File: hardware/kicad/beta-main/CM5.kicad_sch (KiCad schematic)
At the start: 1 part, among them J1 FFC3A20-15-G

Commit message: tweaks and added servo controller
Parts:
- added J2, J3, J4, J5: Servo Socket, symbol Connector:Conn_01x03_Pin
- added Q1: MMBT3906, Package_TO_SOT_SMD:SOT-23, symbol Transistor_BJT:MMBT3906
- added R1, R2, R4, R5: 10k, symbol Device:R
- added R3: 20k, symbol Device:R
- added U1, U2: 74LVC1G126, symbol Beta:74LVC1G126
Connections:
- net 3V3: now also Q1.2 (E), R1.1, R4.1, R5.1, U1.5 (VCC), U2.5 (VCC)
- net GND: now also J2.3 (Pin_3), J3.3 (Pin_3), J4.3 (Pin_3), J5.3 (Pin_3), R3.1, U1.3 (GND), U2.3 (GND)
- new net: J2.1 (Pin_1), J3.1 (Pin_1), J4.1 (Pin_1), J5.1 (Pin_1), R4.2, U1.4, U2.2
- new net: Q1.1 (B), R2.1
- new net 12V: J2.2 (Pin_2), J3.2 (Pin_2), J4.2 (Pin_2), J5.2 (Pin_2)
- new net TXEN: Q1.3 (C), R3.2, U1.1, U2.1
- new net UART3_RX: R5.2, U2.4
- new net UART3_TX: R1.2, R2.2, U1.2
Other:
- sheet GPIO ports: added UART3_RX, UART3_TX; removed none
- note added: "Servo Controller"

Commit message: tweaks
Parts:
- added J6: FFC3A20-15-G, symbol Connector:Conn_01x15_Socket
- U1, U2: Supplier (none) -> https://www.tme.eu/en/details/sn74lvc1g126dbvr/buffers-tran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
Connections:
- net 3V3: now also J6.15 (Pin_15)
- net GND: now also J6.1 (Pin_1), J6.10 (Pin_10), J6.4 (Pin_4), J6.7 (Pin_7)
- new net MIPI1_C_N: J6.8 (Pin_8)
- new net MIPI1_C_P: J6.9 (Pin_9)
- new net MIPI1_D0_N: J6.2 (Pin_2)
- new net MIPI1_D0_P: J6.3 (Pin_3)
- new net MIPI1_D1_N: J6.5 (Pin_5)
- new net MIPI1_D1_P: J6.6 (Pin_6)
- new net SCL1: J6.13 (Pin_13)
- new net SDA1: J6.14 (Pin_14)
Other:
- sheet GPIO ports: added CAM_GPIO0, CAM_GPIO1, SCL1, SDA1; removed none

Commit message: sync changes after meeting
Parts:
- removed J2, J3, J4, J5: Servo Socket, symbol Connector:Conn_01x03_Pin
- removed Q1: MMBT3906, Package_TO_SOT_SMD:SOT-23, symbol Transistor_BJT:MMBT3906
- removed R1, R2, R4, R5: 10k, symbol Device:R
- removed R3: 20k, symbol Device:R
- removed U1, U2: 74LVC1G126, symbol Beta:74LVC1G126
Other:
- note removed: "Servo Controller"

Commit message: Wzmacniacz dodany
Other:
- sheet GPIO ports: added GPIO18, GPIO19, GPIO21; removed none
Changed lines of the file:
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@@
+	(wire
+		(pts
+			(xy 48.26 41.91) (xy 57.15 41.91)
+		)
+		(stroke
+			(width 0)
+			(type default)
+		)
+	)
 	(wire
 		(pts
@@
 	(wire
 		(pts
+			(xy 48.26 44.45) (xy 57.15 44.45)
+		)
+		(stroke
+			(width 0)
+			(type default)
+		)
+	)
+	(wire
+		(pts
 			(xy 231.14 92.71) (xy 241.3 92.71)
 		)
@@
 		(pts
 			(xy 161.29 49.53) (xy 158.75 49.53)
+		)
+		(stroke
+			(width 0)
+			(type default)
+		)
+	)
+	(wire
+		(pts
+			(xy 48.26 39.37) (xy 57.15 39.37)
 		)
 		(stroke
@@
 		)
 	)
+	(hierarchical_label "GPIO18"
+		(shape input)
+		(at 48.26 39.37 180)
+		(effects
+			(font
+				(size 1.27 1.27)
+			)
+			(justify right)
+		)
+	)
 	(hierarchical_label "GND"
 		(shape input)
@@
 		)
 	)
+	(hierarchical_label "GPIO19"
+		(shape input)
+		(at 48.26 41.91 180)
+		(effects
+			(font
+				(size 1.27 1.27)
+			)
+			(justify right)
+		)
+	)
 	(hierarchical_label "5V"
 		(shape input)
 		(at 52.07 54.61 180)
+		(effects
+			(font
+				(size 1.27 1.27)
+			)
+			(justify right)
+		)
+	)
+	(hierarchical_label "GPIO21"
+		(shape input)
+		(at 48.26 44.45 180)
 		(effects
 			(font
@@
 			)
 		)
+		(pin "GPIO19" input
+			(at 57.15 41.91 180)
+			(effects
+				(font
+					(size 1.27 1.27)
+				)
+				(justify left)
+			)
+		)
+		(pin "GPIO18" input
+			(at 57.15 39.37 180)
+			(effects
+				(font
+					(size 1.27 1.27)
+				)
+				(justify left)
+			)
+		)
+		(pin "GPIO21" input
+			(at 57.15 44.45 180)
+			(effects
+				(font
+					(size 1.27 1.27)
+				)
+				(justify left)
+			)
+		)

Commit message: 5V and amplifier corrections
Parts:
- renumbered J6 to J2
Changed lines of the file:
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@@
 		(dnp no)
 		(fields_autoplaced yes)
-		(property "Reference" "J6"
+		(property "Reference" "J2"
 			(at 247.65 104.1399 0)
 			(effects
@@
 			(project "beta-main"
 				(path "/ec75fd42-4efa-4f32-b57e-76d632cb46f5/b3cf40a7-4d41-420e-a440-2c08f4160b31"
-					(reference "J6")
+					(reference "J2")
 					(unit 1)
 				)

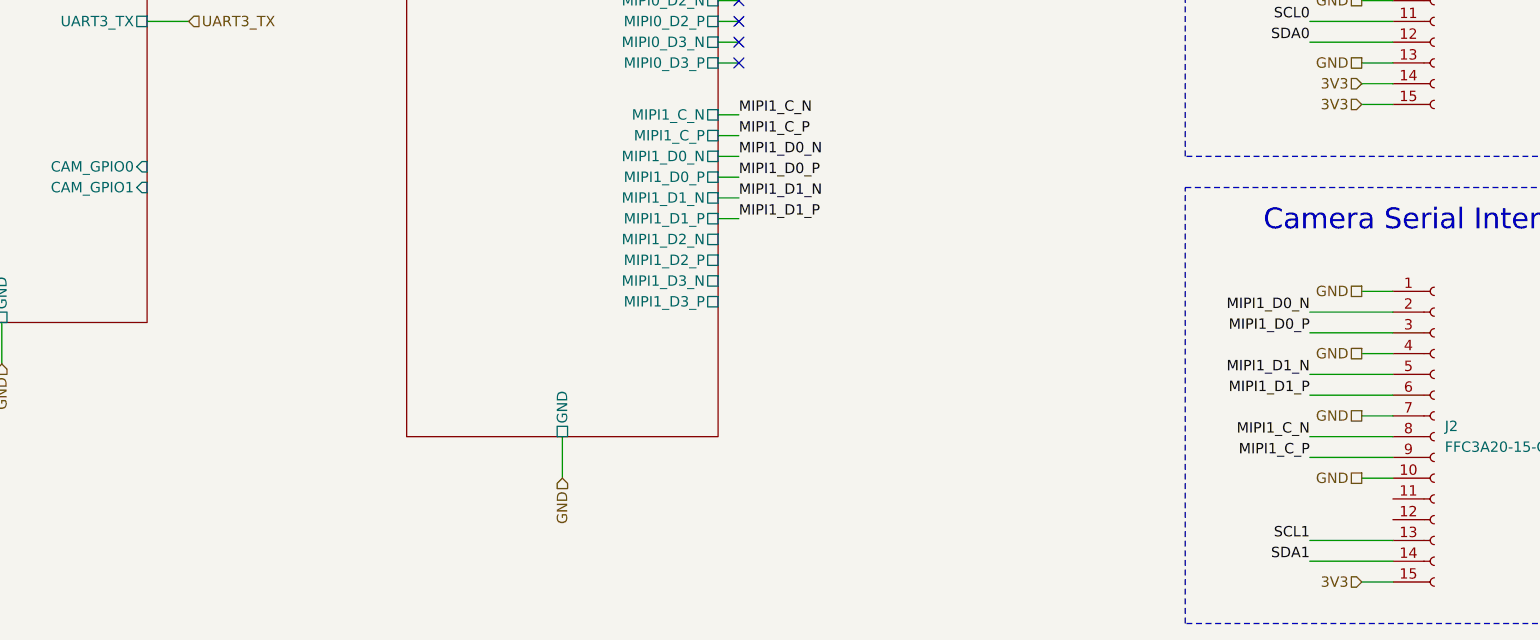
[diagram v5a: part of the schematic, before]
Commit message: Amplifier set for left channel only and god rid of all errors from ERC
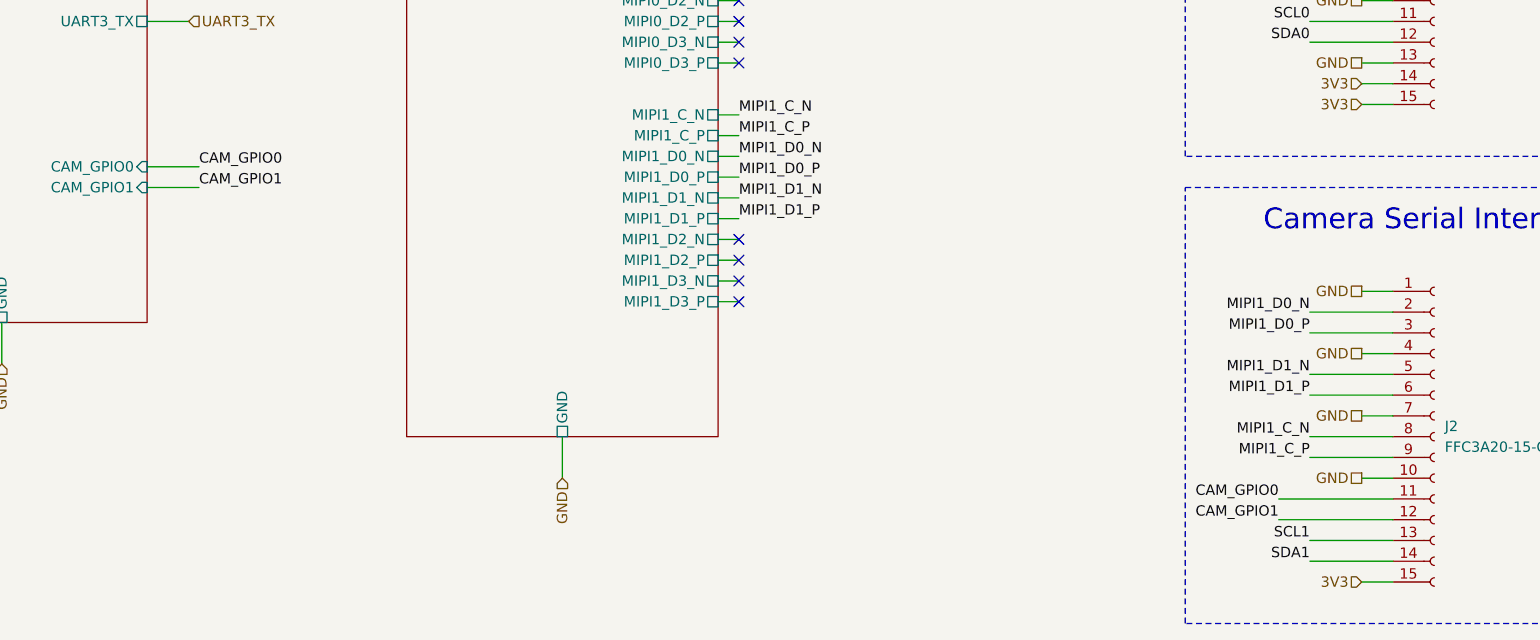
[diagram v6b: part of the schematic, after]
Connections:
- net CAM_GPIO0: now reaches J2.11 (Pin_11)
- net CAM_GPIO1: now reaches J2.12 (Pin_12)
- no-connect marks 4 -> 8
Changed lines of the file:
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@@
+	)
+	(no_connect
+		(at 161.29 88.9)
+	)
+	(no_connect
+		(at 161.29 81.28)
+	)
+	(no_connect
+		(at 161.29 83.82)
+	)
+	(no_connect
+		(at 161.29 86.36)
 	)
 	(no_connect
@@
 	(wire
 		(pts
+			(xy 88.9 74.93) (xy 95.25 74.93)
+		)
+		(stroke
+			(width 0)
+			(type default)
+		)
+	)
+	(wire
+		(pts
+			(xy 88.9 72.39) (xy 95.25 72.39)
+		)
+		(stroke
+			(width 0)
+			(type default)
+		)
+	)
+	(wire
+		(pts
 			(xy 231.14 97.79) (xy 241.3 97.79)
 		)
@@
 	(wire
 		(pts
+			(xy 158.75 81.28) (xy 161.29 81.28)
+		)
+		(stroke
+			(width 0)
+			(type default)
+		)
+	)
+	(wire
+		(pts
 			(xy 231.14 92.71) (xy 241.3 92.71)
 		)
@@
 	(wire
 		(pts
+			(xy 227.33 113.03) (xy 241.3 113.03)
+		)
+		(stroke
+			(width 0)
+			(type default)
+		)
+	)
+	(wire
+		(pts
 			(xy 48.26 39.37) (xy 57.15 39.37)
 		)
@@
 	(wire
 		(pts
+			(xy 158.75 88.9) (xy 161.29 88.9)
+		)
+		(stroke
+			(width 0)
+			(type default)
+		)
+	)
+	(wire
+		(pts
 			(xy 158.75 59.69) (xy 161.29 59.69)
 		)
@@
 	(wire
 		(pts
+			(xy 158.75 86.36) (xy 161.29 86.36)
+		)
+		(stroke
+			(width 0)
+			(type default)
+		)
+	)
+	(wire
+		(pts
 			(xy 161.29 39.37) (xy 158.75 39.37)
 		)
@@
 	(wire
 		(pts
+			(xy 227.33 115.57) (xy 241.3 115.57)
+		)
+		(stroke
+			(width 0)
+			(type default)
+		)
+	)
+	(wire
+		(pts
 			(xy 237.49 110.49) (xy 241.3 110.49)
 		)
@@
 		(pts
 			(xy 237.49 102.87) (xy 241.3 102.87)
+		)
+		(stroke
+			(width 0)
+			(type default)
+		)
+	)
+	(wire
+		(pts
+			(xy 158.75 83.82) (xy 161.29 83.82)
 		)
 		(stroke
@@
 		)
 	)
+	(label "CAM_GPIO0"
+		(at 227.33 113.03 180)
+		(effects
+			(font
+				(size 1.27 1.27)
+			)
+			(justify right bottom)
+		)
+	)
 	(label "MIPI0_C_N"
 		(at 161.29 36.83 0)
@@
 		)
 	)
+	(label "CAM_GPIO0"
+		(at 95.25 72.39 0)
+		(effects
+			(font
+				(size 1.27 1.27)
+			)
+			(justify left bottom)
+		)
+	)
 	(label "SDA1"
 		(at 231.14 120.65 180)
@@
 		)
 	)
+	(label "CAM_GPIO1"
+		(at 95.25 74.93 0)
+		(effects
+			(font
+				(size 1.27 1.27)
+			)
+			(justify left bottom)
+		)
+	)
 	(label "MIPI1_D0_P"
 		(at 231.14 92.71 180)
@@
 		)
 	)
+	(label "CAM_GPIO1"
+		(at 227.33 115.57 180)
+		(effects
+			(font
+				(size 1.27 1.27)
+			)
+			(justify right bottom)
+		)
+	)

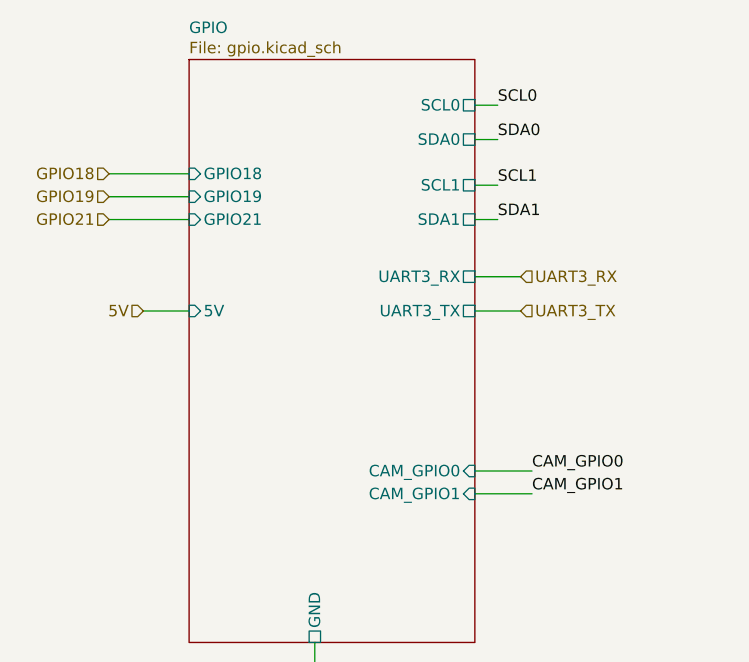
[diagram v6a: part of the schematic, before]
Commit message: Gyroscope added without errors in ERC
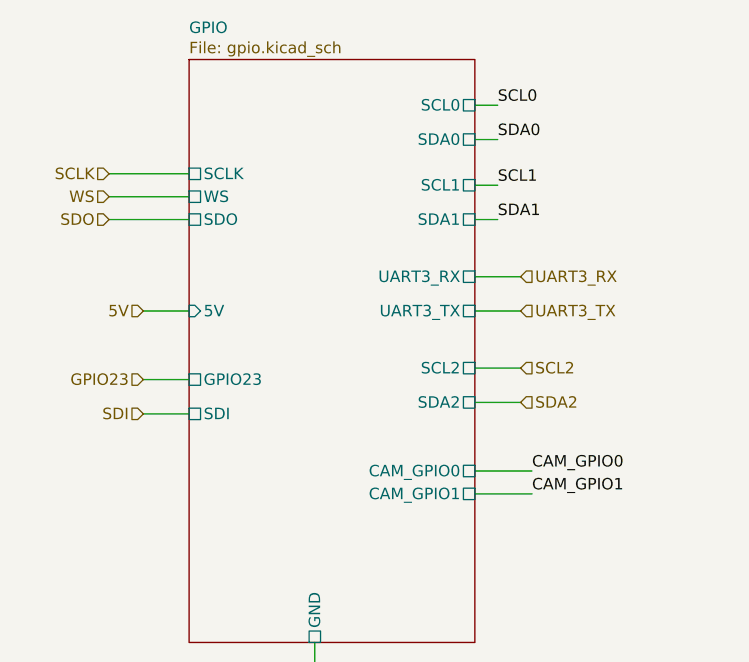
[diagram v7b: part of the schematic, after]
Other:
- sheet GPIO ports: added GPIO23, SCL2, SCLK, SDA2, SDI, SDO, WS; removed GPIO18, GPIO19, GPIO21
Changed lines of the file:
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@@
+	(wire
+		(pts
+			(xy 93.98 64.77) (xy 88.9 64.77)
+		)
+		(stroke
+			(width 0)
+			(type default)
+		)
+	)
 	(wire
 		(pts
@@
 	(wire
 		(pts
+			(xy 52.07 66.04) (xy 57.15 66.04)
+		)
+		(stroke
+			(width 0)
+			(type default)
+		)
+	)
+	(wire
+		(pts
 			(xy 158.75 59.69) (xy 161.29 59.69)
 		)
@@
 		(pts
 			(xy 158.75 83.82) (xy 161.29 83.82)
+		)
+		(stroke
+			(width 0)
+			(type default)
+		)
+	)
+	(wire
+		(pts
+			(xy 52.07 62.23) (xy 57.15 62.23)
+		)
+		(stroke
+			(width 0)
+			(type default)
+		)
+	)
+	(wire
+		(pts
+			(xy 88.9 60.96) (xy 93.98 60.96)
 		)
 		(stroke
@@
 		)
 	)
+	(hierarchical_label "GPIO23"
+		(shape input)
+		(at 52.07 62.23 180)
+		(effects
+			(font
+				(size 1.27 1.27)
+			)
+			(justify right)
+		)
+	)
+	(hierarchical_label "SDA2"
+		(shape input)
+		(at 93.98 64.77 0)
+		(effects
+			(font
+				(size 1.27 1.27)
+			)
+			(justify left)
+		)
+	)
 	(hierarchical_label "GND"
 		(shape passive)
@@
 		)
 	)
-	(hierarchical_label "GPIO18"
+	(hierarchical_label "SCLK"
 		(shape input)
 		(at 48.26 39.37 180)
@@
 		)
 	)
+	(hierarchical_label "SDI"
+		(shape input)
+		(at 52.07 66.04 180)
+		(effects
+			(font
+				(size 1.27 1.27)
+			)
+			(justify right)
+		)
+	)
 	(hierarchical_label "3V3"
 		(shape input)
@@
 		)
 	)
-	(hierarchical_label "GPIO19"
+	(hierarchical_label "WS"
 		(shape input)
 		(at 48.26 41.91 180)
@@
 		)
 	)
-	(hierarchical_label "GPIO21"
+	(hierarchical_label "SDO"
 		(shape input)
 		(at 48.26 44.45 180)
@@
 		(shape input)
 		(at 93.98 54.61 0)
+		(effects
+			(font
+				(size 1.27 1.27)
+			)
+			(justify left)
+		)
+	)
+	(hierarchical_label "SCL2"
+		(shape input)
+		(at 93.98 60.96 0)
 		(effects
 			(font
@@
 			)
 		)
-		(pin "CAM_GPIO0" input
-			(at 88.9 72.39 0)
-			(effects
-				(font
-					(size 1.27 1.27)
-				)
-				(justify right)
-			)
-		)
-		(pin "CAM_GPIO1" input
-			(at 88.9 74.93 0)
-			(effects
-				(font
-					(size 1.27 1.27)
-				)
-				(justify right)
-			)
-		)
 		(pin "SCL1" passive
 			(at 88.9 40.64 0)
@@
 			)
 		)
-		(pin "GPIO19" input
+		(pin "SDA2" passive
+			(at 88.9 64.77 0)
+			(effects
+				(font
+					(size 1.27 1.27)
+				)
+				(justify right)
+			)
+		)
+		(pin "SCL2" passive
+			(at 88.9 60.96 0)
+			(effects
+				(font
+					(size 1.27 1.27)
+				)
+				(justify right)
+			)
+		)
+		(pin "SCLK" passive
+			(at 57.15 39.37 180)
+			(effects
+				(font
+					(size 1.27 1.27)
+				)
+				(justify left)
+			)
+		)
+		(pin "WS" passive
 			(at 57.15 41.91 180)
 			(effects
@@
 			)
 		)
-		(pin "GPIO18" input
-			(at 57.15 39.37 180)
+		(pin "SDO" passive
+			(at 57.15 44.45 180)
 			(effects
 				(font
@@
 			)
 		)
-		(pin "GPIO21" input
-			(at 57.15 44.45 180)
-			(effects
-				(font
+		(pin "CAM_GPIO0" passive
+			(at 88.9 72.39 0)
+			(effects
+				(font
+					(size 1.27 1.27)
+				)
+				(justify right)
+			)
+		)
+		(pin "CAM_GPIO1" passive
+			(at 88.9 74.93 0)
+			(effects
+				(font
+					(size 1.27 1.27)
+				)
+				(justify right)
+			)
+		)
+		(pin "GPIO23" passive
+			(at 57.15 62.23 180)
+			(effects
+				(font
+					(size 1.27 1.27)
+				)
+				(justify left)
+			)
+		)
+		(pin "SDI" passive
+			(at 57.15 66.04 180)
+			(effects
+				(font

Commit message: Setup for PCB layout
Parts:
- J1, J2: footprint (none) -> Connector_FFC-FPC:TE_1-84953-5_1x15-1MP_P1.0mm_Horizontal
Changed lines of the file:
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@@
 			)
 		)
-		(property "Footprint" ""
+		(property "Footprint" "Connector_FFC-FPC:TE_1-84953-5_1x15-1MP_P1.0mm_Horizontal"
 			(at 246.38 46.99 0)
 			(effects
@@
 			)
 		)
-		(property "Footprint" ""
+		(property "Footprint" "Connector_FFC-FPC:TE_1-84953-5_1x15-1MP_P1.0mm_Horizontal"
 			(at 246.38 105.41 0)
 			(effects
